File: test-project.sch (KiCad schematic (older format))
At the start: 36 parts, among them P1 CONN_01X06, P2 CONN_01X02, U1 74HC14, U2 OP275, U3 74LS163, U4 27C512

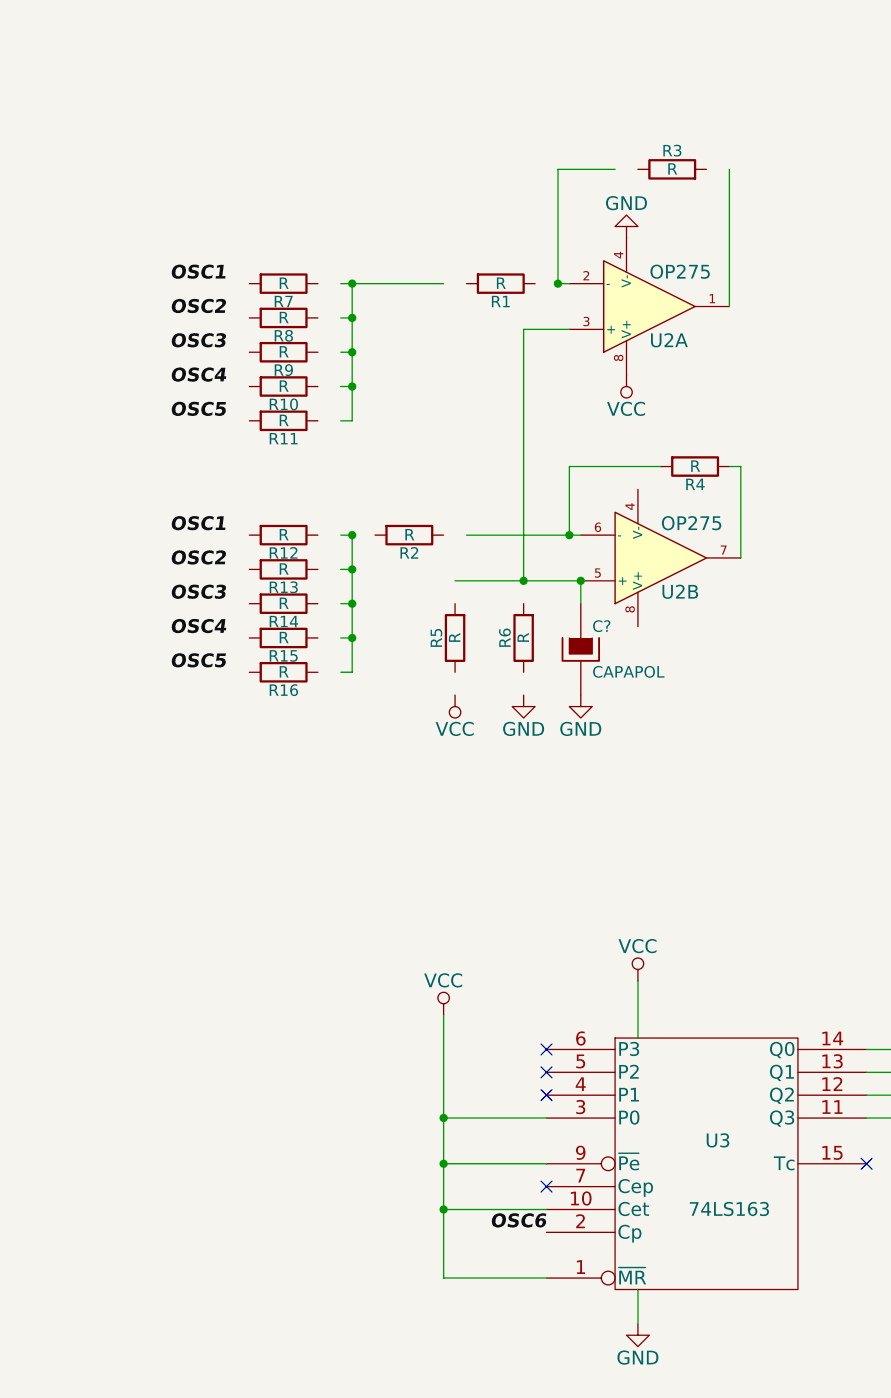
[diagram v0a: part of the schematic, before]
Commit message: Revert changes made assuming incorrect kicad libraries
This reverts commit 3a16a8136e794e249657d61b4e54a01cd5eb9d61.
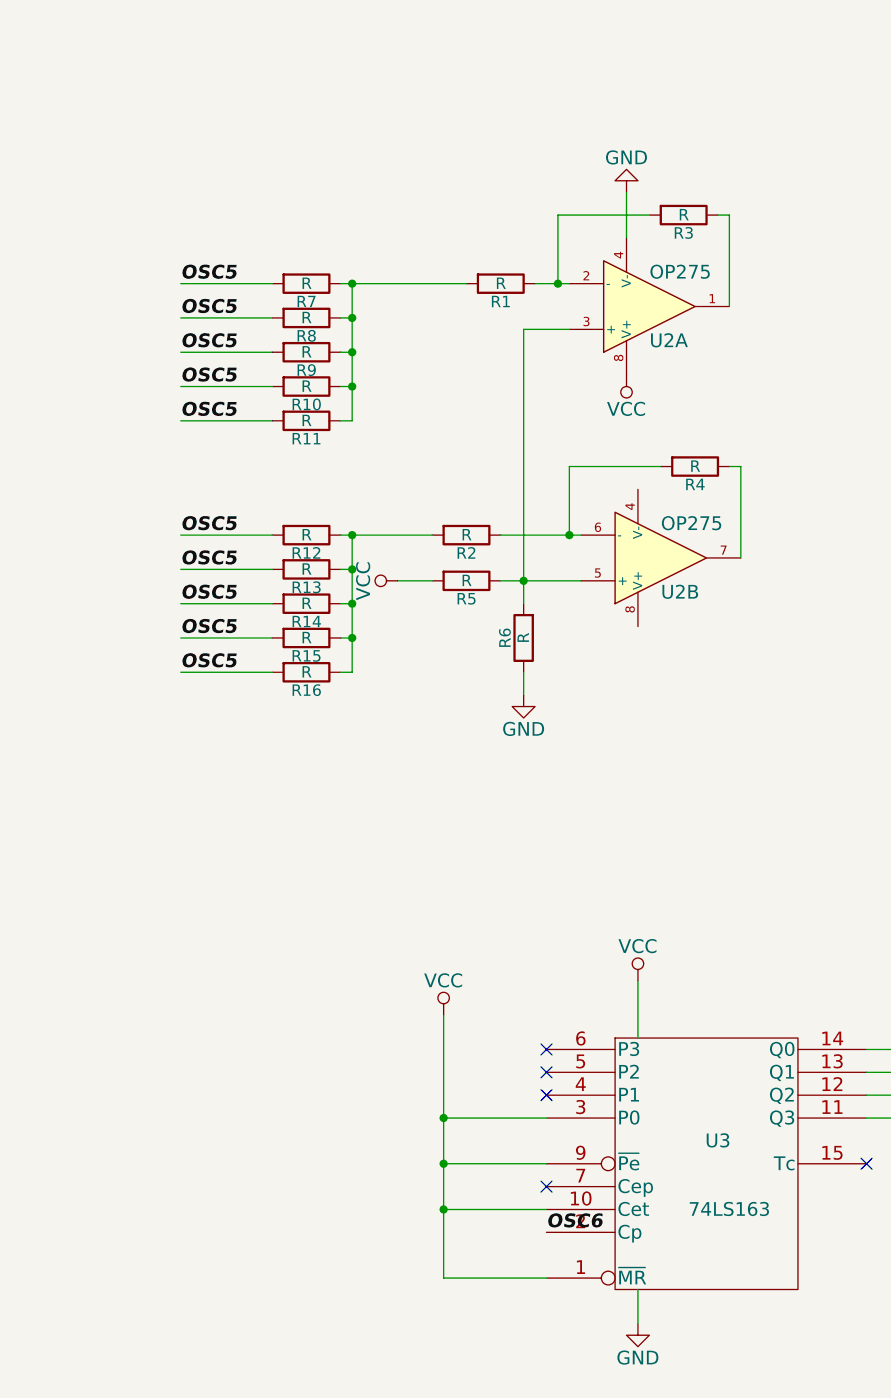
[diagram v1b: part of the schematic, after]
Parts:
- removed C?: CAPAPOL, symbol CAPAPOL
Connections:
- wire segments 80 -> 93
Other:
- moved on the sheet: R10, R11, R12, R13, R14, R15, R16, R2, R3, R5, R7, R8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

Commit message: major details and new parts to EPROM
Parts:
- removed RV2, RV3, RV4, RV5, RV6: POT, Potentiometers:Potentiometer_Trimmer-Piher_PT15-B_vertical, symbol POT
- removed U4: 27C512, symbol 27C512
- added C? (x2): 0.1uF, symbol C
- added P?: CONN_01X08, symbol CONN_01X08
- added RR? (x2): RR6, symbol RR6
- added RV? (x5): 20K, Potentiometers:Potentiometer_Trimmer-Piher_PT15-B_vertical, symbol POT
- added U4: 27C512-DIP, symbol 27C512-DIP
- C1, C2, C3, C5, C6: value CP -> 1uF
- C4, C7: value CP -> 470uF
- RV1: value POT -> 20K
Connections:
- wire segments 93 -> 122
- no-connect marks 17 -> 5
